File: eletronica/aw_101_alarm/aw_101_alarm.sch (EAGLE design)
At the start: 39 parts, among them IC1 ATTINY2313V, IC2 4511N, T2 2N2222, T3 2N2222, T4 2N2222, T5 2N2222, T6 2N2222, X1 UPDOWN, X2 TIMER, X3 STOPBTN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

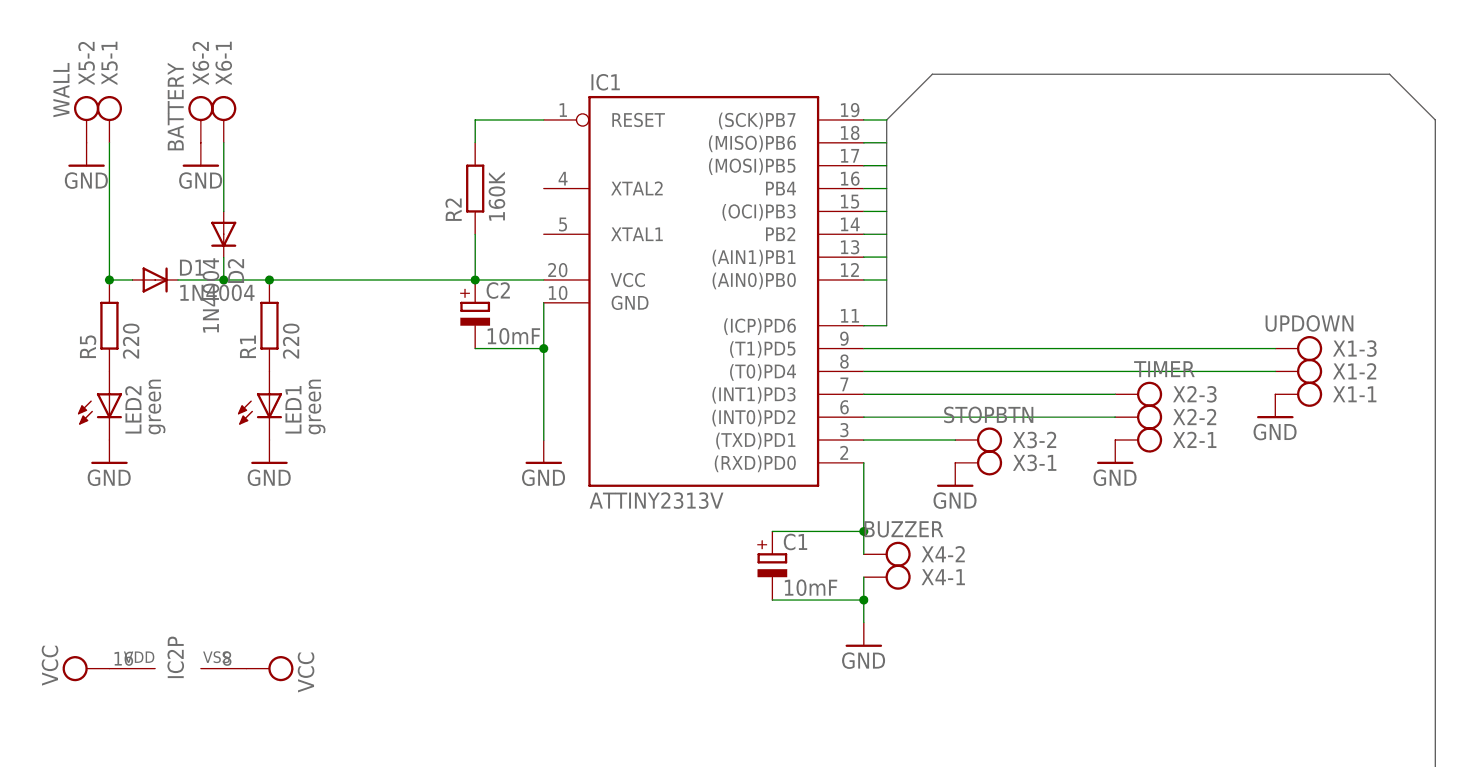
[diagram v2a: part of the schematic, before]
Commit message: 
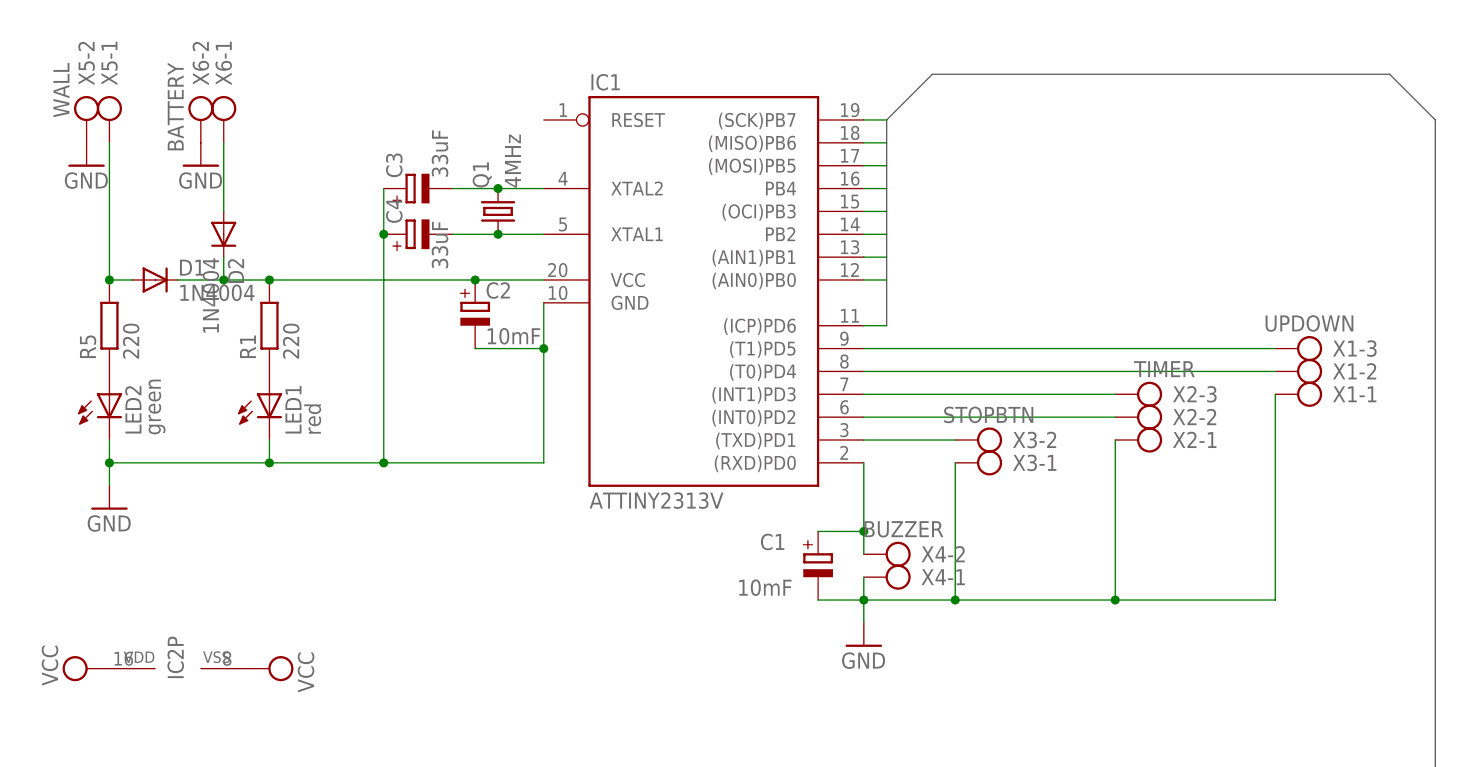
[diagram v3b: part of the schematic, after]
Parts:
- removed R2: 160K, rcl:R-EU_0207/10
- added C3, C4: 33uF, rcl:CPOL-EUE2.5-6
- added Q1: 4MHz, crystal:CRYSTALHC49U70
- LED1: value green -> red
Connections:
- new net N$11: C3.-, IC1.XTAL2, Q1.2
- net GND: now also C3.+, C4.+
- net N$5: now also C4.-, IC1.XTAL1, Q1.1; no longer IC1.RESET, R2.2
- net VCC: no longer R2.1
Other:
- moved on the sheet: C1
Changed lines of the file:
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@@
 <parts>
 <part name="R1" library="rcl" deviceset="R-EU_" device="0207/10" value="220"/>
-<part name="LED1" library="led" deviceset="LED" device="5MM" value="green"/>
-<part name="GND2" library="supply1" deviceset="GND" device=""/>
+<part name="LED1" library="led" deviceset="LED" device="5MM" value="red"/>
 <part name="IC1" library="atmel" deviceset="AT90S2313" device="P" value="ATTINY2313V"/>
-<part name="R2" library="rcl" deviceset="R-EU_" device="0207/10" value="160K"/>
-<part name="GND3" library="supply1" deviceset="GND" device=""/>
 <part name="X1" library="con-ptr500" deviceset="AK500/3" device="" value="UPDOWN"/>
-<part name="GND4" library="supply1" deviceset="GND" device=""/>
 <part name="X2" library="con-ptr500" deviceset="AK500/3" device="" value="TIMER"/>
-<part name="GND5" library="supply1" deviceset="GND" device=""/>
 <part name="X3" library="con-ptr500" deviceset="AK500/2" device="" value="STOPBTN"/>
-<part name="GND6" library="supply1" deviceset="GND" device=""/>
 <part name="C2" library="rcl" deviceset="CPOL-EU" device="E2.5-6" value="10mF"/>
 <part name="IC2" library="45xx" deviceset="4511" device="N"/>
@@
 <part name="X4" library="con-ptr500" deviceset="AK500/2" device="" value="BUZZER"/>
 <part name="C1" library="rcl" deviceset="CPOL-EU" device="E2.5-6" value="10mF"/>
+<part name="Q1" library="crystal" deviceset="CRYSTAL" device="HC49U70" value="4MHz"/>
+<part name="C3" library="rcl" deviceset="CPOL-EU" device="E2.5-6" value="33uF"/>
+<part name="C4" library="rcl" deviceset="CPOL-EU" device="E2.5-6" value="33uF"/>
 </parts>
 <sheets>
@@
 <instance part="R1" gate="G$1" x="20.32" y="55.88" rot="R90"/>
 <instance part="LED1" gate="G$1" x="20.32" y="48.26"/>
-<instance part="GND2" gate="1" x="20.32" y="40.64"/>
 <instance part="IC1" gate="G$1" x="68.58" y="58.42"/>
-<instance part="R2" gate="G$1" x="43.18" y="71.12" rot="R90"/>
-<instance part="GND3" gate="1" x="50.8" y="40.64"/>
 <instance part="X1" gate="-1" x="137.16" y="48.26" rot="R180"/>
 <instance part="X1" gate="-2" x="137.16" y="50.8" rot="R180"/>
 <instance part="X1" gate="-3" x="137.16" y="53.34" rot="R180"/>
-<instance part="GND4" gate="1" x="132.08" y="45.72"/>
 <instance part="X2" gate="-1" x="119.38" y="43.18" rot="R180"/>
 <instance part="X2" gate="-2" x="119.38" y="45.72" rot="R180"/>
 <instance part="X2" gate="-3" x="119.38" y="48.26" rot="R180"/>
-<instance part="GND5" gate="1" x="114.3" y="40.64"/>
 <instance part="X3" gate="-1" x="101.6" y="40.64" rot="R180"/>
 <instance part="X3" gate="-2" x="101.6" y="43.18" rot="R180"/>
-<instance part="GND6" gate="1" x="96.52" y="38.1"/>
 <instance part="C2" gate="G$1" x="43.18" y="58.42"/>
 <instance part="IC2" gate="A" x="27.94" y="-17.78"/>
@@
 <instance part="R5" gate="G$1" x="2.54" y="55.88" rot="R90"/>
 <instance part="LED2" gate="G$1" x="2.54" y="48.26"/>
-<instance part="GND1" gate="1" x="2.54" y="40.64"/>
+<instance part="GND1" gate="1" x="2.54" y="35.56"/>
 <instance part="D1" gate="1" x="7.62" y="60.96"/>
 <instance part="D2" gate="1" x="15.24" y="66.04" rot="R270"/>
@@
 <instance part="X4" gate="-1" x="91.44" y="27.94" rot="R180"/>
 <instance part="X4" gate="-2" x="91.44" y="30.48" rot="R180"/>
-<instance part="C1" gate="G$1" x="76.2" y="30.48"/>
+<instance part="C1" gate="G$1" x="81.28" y="30.48" smashed="yes">
+<attribute name="NAME" x="74.803" y="30.9626" size="1.778" layer="95"/>
+<attribute name="VALUE" x="72.263" y="25.8826" size="1.778" layer="96"/>
+</instance>
+<instance part="Q1" gate="G$1" x="45.72" y="68.58" rot="R90"/>
+<instance part="C3" gate="G$1" x="35.56" y="71.12" rot="R90"/>
+<instance part="C4" gate="G$1" x="35.56" y="66.04" smashed="yes" rot="R90">
+<attribute name="NAME" x="35.0774" y="67.183" size="1.778" layer="95" rot="R90"/>
+<attribute name="VALUE" x="40.1574" y="62.103" size="1.778" layer="96" rot="R90"/>
+</instance>
 </instances>
 <busses>
@@
 <nets>
 <net name="GND" class="0">
-<segment>
-<pinref part="LED1" gate="G$1" pin="C"/>
-<pinref part="GND2" gate="1" pin="GND"/>
-</segment>
-<segment>
-<pinref part="IC1" gate="G$1" pin="GND"/>
-<pinref part="GND3" gate="1" pin="GND"/>
-<wire x1="50.8" y1="58.42" x2="50.8" y2="53.34" width="0.1524" layer="91"/>
-<pinref part="C2" gate="G$1" pin="-"/>
-<wire x1="50.8" y1="53.34" x2="50.8" y2="43.18" width="0.1524" layer="91"/>
-<wire x1="43.18" y1="53.34" x2="50.8" y2="53.34" width="0.1524" layer="91"/>
-<junction x="50.8" y="53.34"/>
-</segment>
-<segment>
-<pinref part="X1" gate="-1" pin="KL"/>
-<pinref part="GND4" gate="1" pin="GND"/>
-</segment>
-<segment>
-<pinref part="X2" gate="-1" pin="KL"/>
-<pinref part="GND5" gate="1" pin="GND"/>
-</segment>
-<segment>
-<pinref part="X3" gate="-1" pin="KL"/>
-<pinref part="GND6" gate="1" pin="GND"/>
-</segment>
 <segment>
 <pinref part="IC2" gate="A" pin="LE"/>
@@
 <pinref part="LED2" gate="G$1" pin="C"/>
 <pinref part="GND1" gate="1" pin="GND"/>
+<wire x1="2.54" y1="38.1" x2="2.54" y2="40.64" width="0.1524" layer="91"/>
+<pinref part="LED1" gate="G$1" pin="C"/>
+<wire x1="2.54" y1="40.64" x2="2.54" y2="43.18" width="0.1524" layer="91"/>
+<wire x1="20.32" y1="43.18" x2="20.32" y2="40.64" width="0.1524" layer="91"/>
+<pinref part="IC1" gate="G$1" pin="GND"/>
+<wire x1="50.8" y1="58.42" x2="50.8" y2="53.34" width="0.1524" layer="91"/>
+<pinref part="C2" gate="G$1" pin="-"/>
+<wire x1="50.8" y1="53.34" x2="50.8" y2="40.64" width="0.1524" layer="91"/>
+<wire x1="43.18" y1="53.34" x2="50.8" y2="53.34" width="0.1524" layer="91"/>
+<junction x="50.8" y="53.34"/>
+<wire x1="50.8" y1="40.64" x2="33.02" y2="40.64" width="0.1524" layer="91"/>
+<pinref part="C3" gate="G$1" pin="+"/>
+<pinref part="C4" gate="G$1" pin="+"/>
+<wire x1="33.02" y1="40.64" x2="20.32" y2="40.64" width="0.1524" layer="91"/>
+<wire x1="33.02" y1="71.12" x2="33.02" y2="66.04" width="0.1524" layer="91"/>
+<wire x1="33.02" y1="66.04" x2="33.02" y2="40.64" width="0.1524" layer="91"/>
+<junction x="33.02" y="66.04"/>
+<junction x="33.02" y="40.64"/>
+<wire x1="20.32" y1="40.64" x2="2.54" y2="40.64" width="0.1524" layer="91"/>
+<junction x="20.32" y="40.64"/>
+<junction x="2.54" y="40.64"/>
 </segment>
 <segment>
@@
 <pinref part="C1" gate="G$1" pin="-"/>
 <wire x1="86.36" y1="25.4" x2="86.36" y2="27.94" width="0.1524" layer="91"/>
-<wire x1="76.2" y1="25.4" x2="86.36" y2="25.4" width="0.1524" layer="91"/>
+<wire x1="81.28" y1="25.4" x2="86.36" y2="25.4" width="0.1524" layer="91"/>
 <junction x="86.36" y="25.4"/>
+<pinref part="X3" gate="-1" pin="KL"/>
+<wire x1="96.52" y1="40.64" x2="96.52" y2="25.4" width="0.1524" layer="91"/>
+<wire x1="96.52" y1="25.4" x2="86.36" y2="25.4" width="0.1524" layer="91"/>
+<pinref part="X2" gate="-1" pin="KL"/>
+<wire x1="114.3" y1="43.18" x2="114.3" y2="25.4" width="0.1524" layer="91"/>
+<wire x1="114.3" y1="25.4" x2="96.52" y2="25.4" width="0.1524" layer="91"/>
+<junction x="96.52" y="25.4"/>
+<pinref part="X1" gate="-1" pin="KL"/>
+<wire x1="132.08" y1="48.26" x2="132.08" y2="25.4" width="0.1524" layer="91"/>
+<wire x1="132.08" y1="25.4" x2="114.3" y2="25.4" width="0.1524" layer="91"/>
+<junction x="114.3" y="25.4"/>
 </segment>
 </net>
@@
 <wire x1="43.18" y1="60.96" x2="50.8" y2="60.96" width="0.1524" layer="91"/>
 <junction x="43.18" y="60.96"/>
-<pinref part="R2" gate="G$1" pin="1"/>
-<wire x1="43.18" y1="60.96" x2="43.18" y2="66.04" width="0.1524" layer="91"/>
 <pinref part="D2" gate="1" pin="C"/>
 <pinref part="D1" gate="1" pin="C"/>
@@
 <pinref part="R1" gate="G$1" pin="1"/>
 <pinref part="LED1" gate="G$1" pin="A"/>
-</segment>
-</net>
-<net name="N$5" class="0">
-<segment>
-<pinref part="IC1" gate="G$1" pin="RESET"/>
-<pinref part="R2" gate="G$1" pin="2"/>
-<wire x1="50.8" y1="78.74" x2="43.18" y2="78.74" width="0.1524" layer="91"/>
-<wire x1="43.18" y1="78.74" x2="43.18" y2="76.2" width="0.1524" layer="91"/>
 </segment>
 </net>
@@
 <pinref part="C1" gate="G$1" pin="+"/>
 <wire x1="86.36" y1="33.02" x2="86.36" y2="30.48" width="0.1524" layer="91"/>
-<wire x1="76.2" y1="33.02" x2="86.36" y2="33.02" width="0.1524" layer="91"/>
+<wire x1="81.28" y1="33.02" x2="86.36" y2="33.02" width="0.1524" layer="91"/>
 <junction x="86.36" y="33.02"/>
 </segment>
 </net>
+<net name="N$5" class="0">
+<segment>
+<pinref part="IC1" gate="G$1" pin="XTAL1"/>
+<pinref part="Q1" gate="G$1" pin="1"/>
+<wire x1="50.8" y1="66.04" x2="45.72" y2="66.04" width="0.1524" layer="91"/>
+<pinref part="C4" gate="G$1" pin="-"/>
+<wire x1="45.72" y1="66.04" x2="40.64" y2="66.04" width="0.1524" layer="91"/>
+<junction x="45.72" y="66.04"/>
+</segment>
+</net>
+<net name="N$11" class="0">
+<segment>
+<pinref part="IC1" gate="G$1" pin="XTAL2"/>
+<pinref part="Q1" gate="G$1" pin="2"/>
+<wire x1="50.8" y1="71.12" x2="45.72" y2="71.12" width="0.1524" layer="91"/>
+<pinref part="C3" gate="G$1" pin="-"/>
+<wire x1="45.72" y1="71.12" x2="40.64" y2="71.12" width="0.1524" layer="91"/>
+<junction x="45.72" y="71.12"/>
+</segment>
+</net>
